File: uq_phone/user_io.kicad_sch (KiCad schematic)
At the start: 27 parts, among them J7 Conn_01x02, J8 KP15B-6S-SF_800_, J9 541324562, M1 VCDM0834B004L, U10 TPD3F303DQDR, U11 TPD8F003DQDR, U12 MCP1664T-E/OT, U8 LSM6DSVTR, U9 DRV2603RUNR

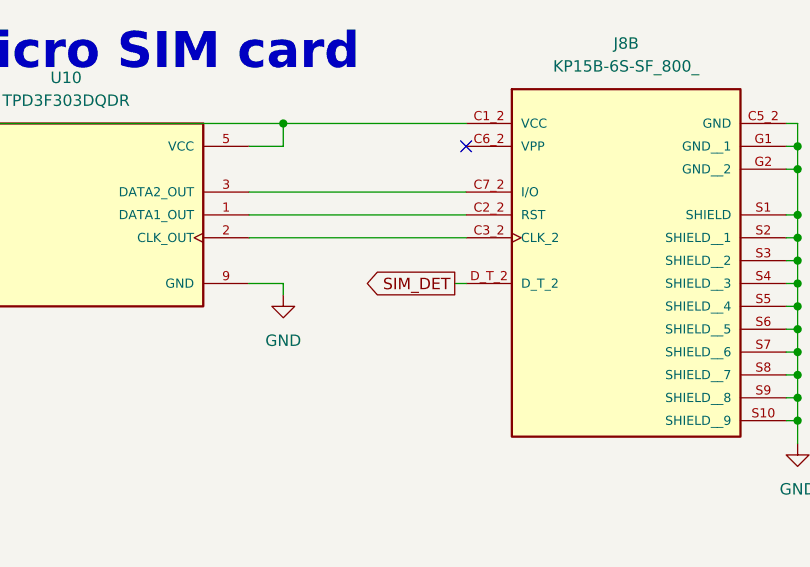
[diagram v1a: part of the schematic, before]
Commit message: Update pcb and remove Stm32 profile
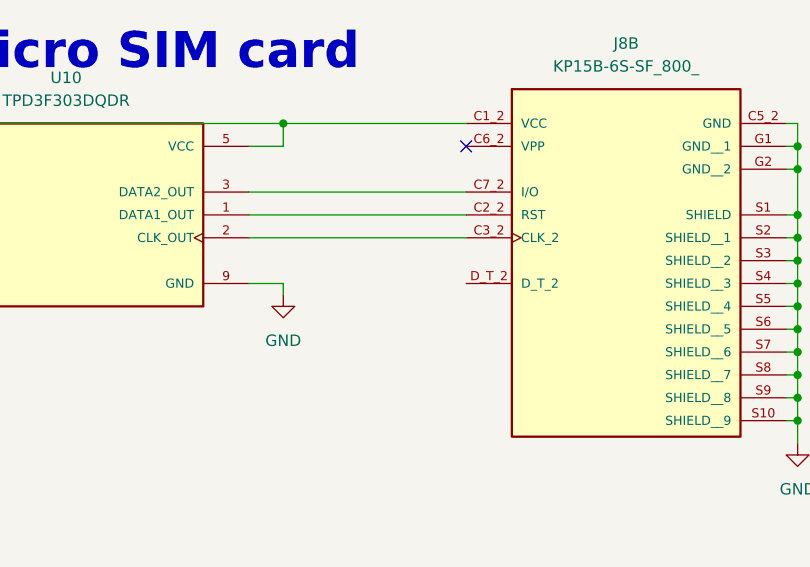
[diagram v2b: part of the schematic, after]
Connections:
- net SIM_DET: no longer names the net of J8.D_T_2
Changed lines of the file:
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@@
-	(wire
-		(pts
-			(xy 175.26 143.51) (xy 176.53 143.51)
-		)
-		(stroke
-			(width 0)
-			(type default)
-		)
-	)
 	(wire
 		(pts
@@
 			(effects
 				(font
-					(size 1.27 1.27)
-				)
-				(justify right)
-				(hide yes)
-			)
-		)
-	)
-	(global_label "SIM_DET"
-		(shape output)
-		(at 175.26 143.51 180)
-		(fields_autoplaced yes)
-		(effects
-			(font
-				(size 1.27 1.27)
-			)
-			(justify right)
-		)
-		(property "Intersheetrefs" "${INTERSHEET_REFS}"
-			(at 164.6549 143.51 0)
-			(effects
-				(font

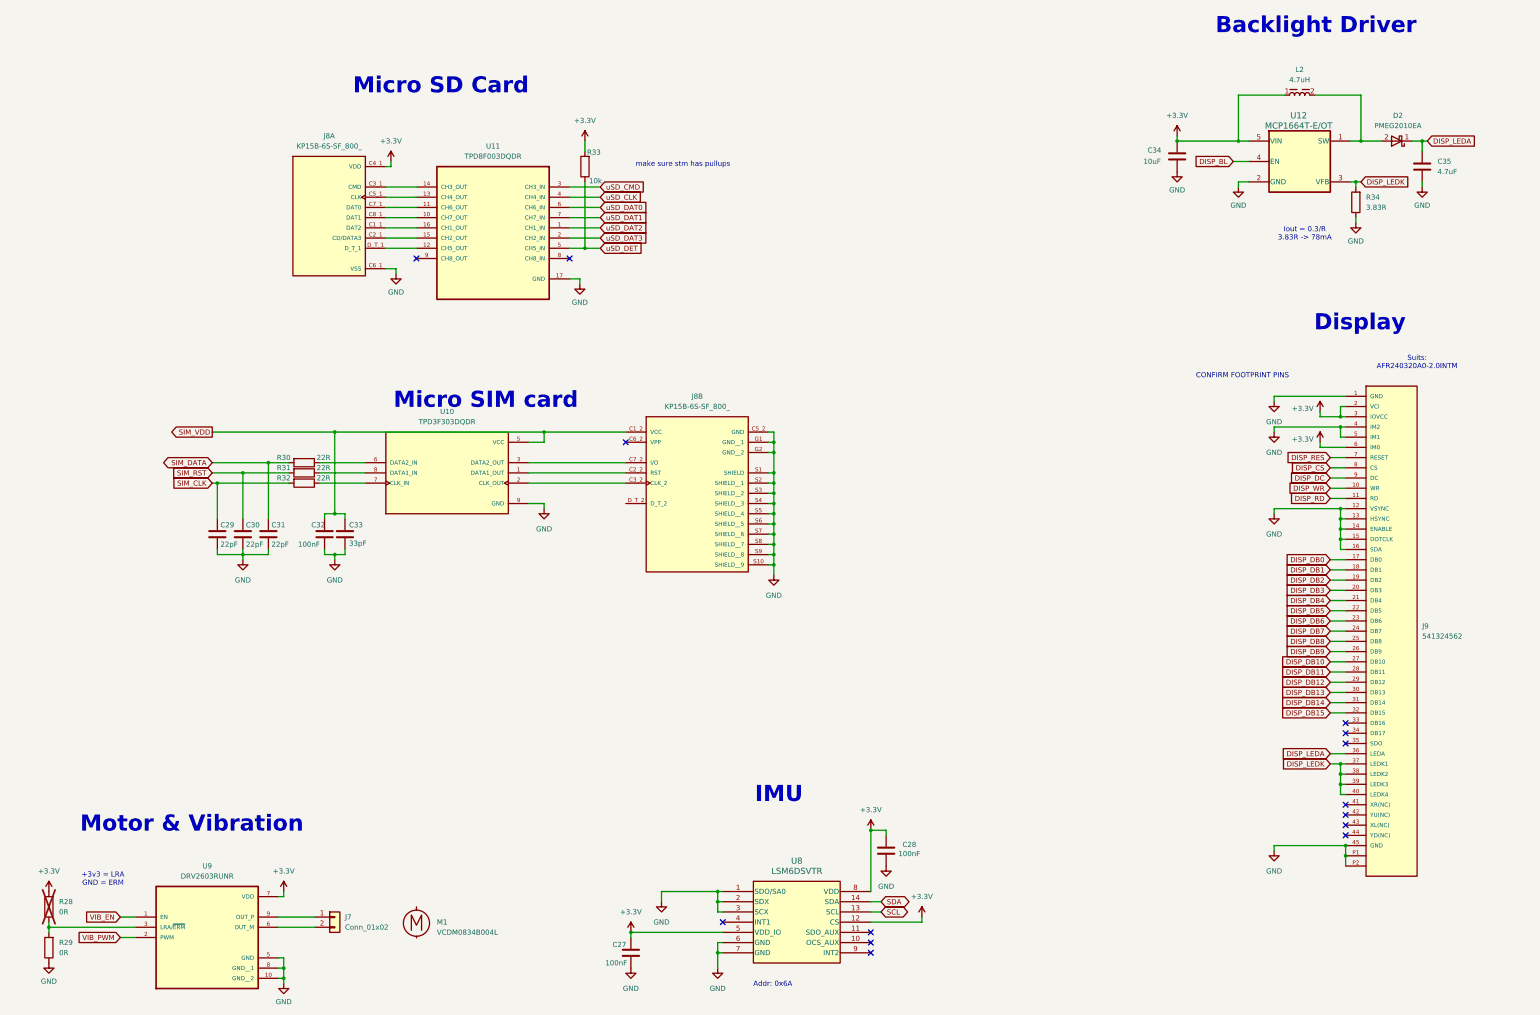
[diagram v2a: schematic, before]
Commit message: Add Front Pannel Suboard and connector
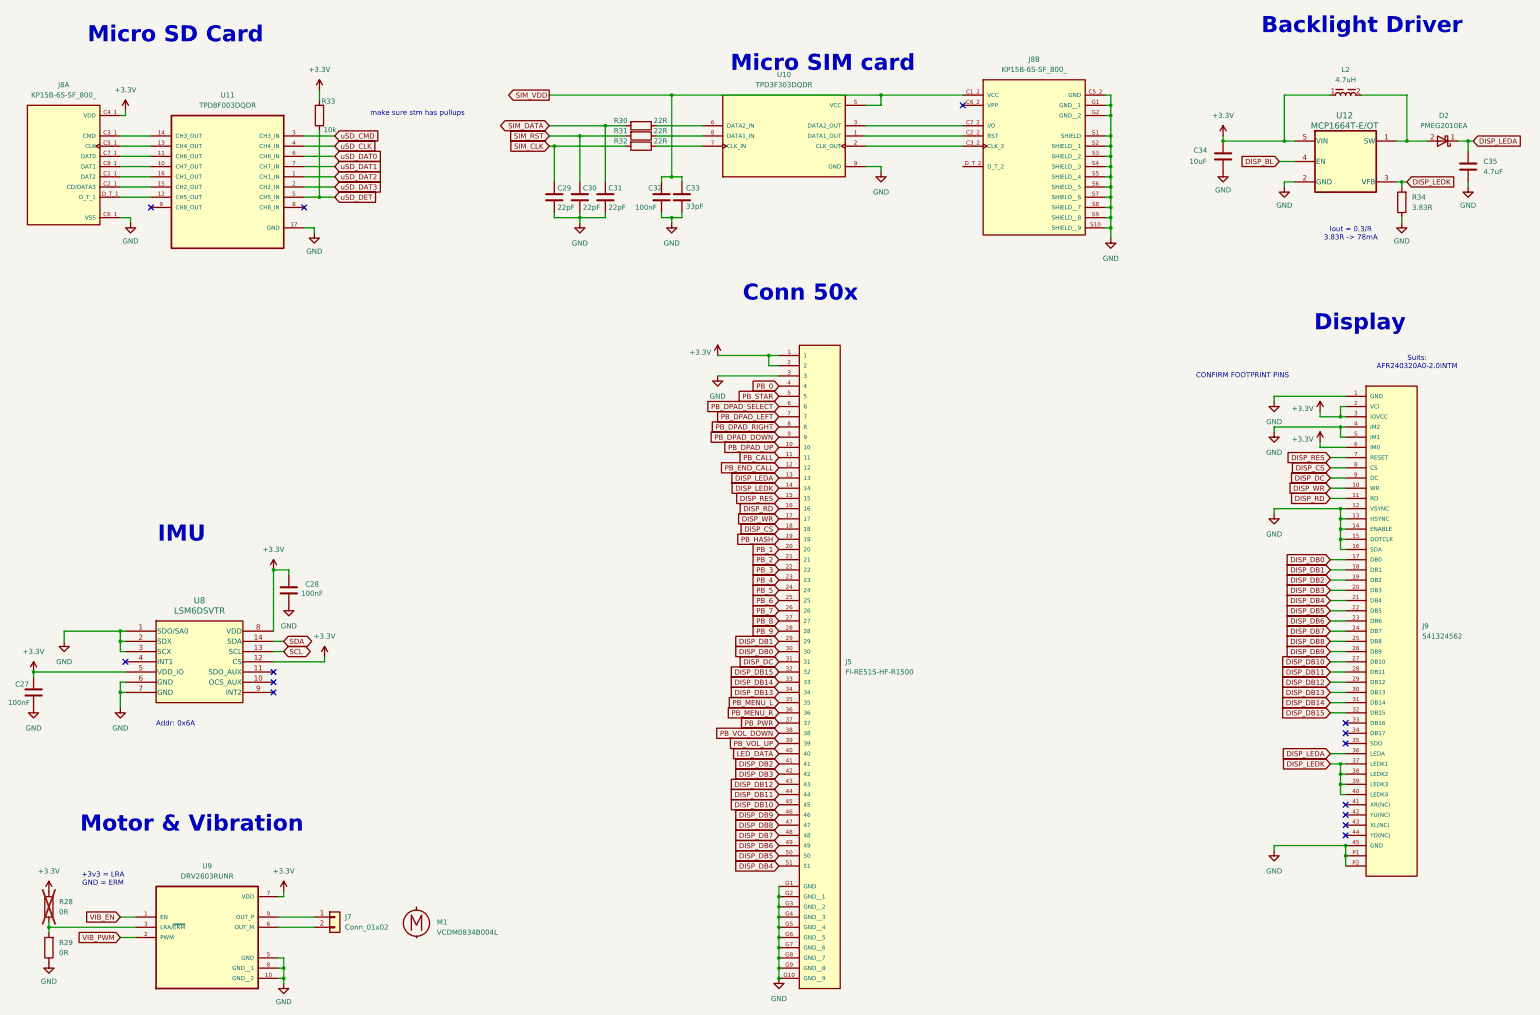
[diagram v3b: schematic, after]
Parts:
- added J5: FI-RE51S-HF-R1500, FI-RE51S-HF-R1500:JAE_FI-RE51S-HF-R1500, symbol FI-RE51S-HF-R1500:FI-RE51S-HF-R1500
- J9: now left out of the parts list
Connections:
- net +3.3V: now also J5.1, J5.2
- net DISP_CS: now also J5.18
- net DISP_DB0: now also J5.30
- net DISP_DB1: now also J5.29
- net DISP_DB10: now also J5.45
- net DISP_DB11: now also J5.44
- net DISP_DB12: now also J5.43
- net DISP_DB13: now also J5.34
- net DISP_DB14: now also J5.33
- net DISP_DB15: now also J5.32
- net DISP_DB2: now also J5.41
- net DISP_DB3: now also J5.42
- net DISP_DB4: now also J5.51
- net DISP_DB5: now also J5.50
- net DISP_DB6: now also J5.49
- net DISP_DB7: now also J5.48
- net DISP_DB8: now also J5.47
- net DISP_DB9: now also J5.46
- net DISP_DC: now also J5.31
- net DISP_LEDA: now also J5.13
- net DISP_LEDK: now also J5.14
- net DISP_RD: now also J5.16
- net DISP_RES: now also J5.15
- net DISP_WR: now also J5.17
- net GND: now also J5.3, J5.G1 (GND), J5.G10 (GND__9), J5.G2 (GND__1), J5.G3 (GND__2), J5.G4 (GND__3), J5.G5 (GND__4), J5.G6 (GND__5), J5.G7 (GND__6), J5.G8 (GND__7), J5.G9 (GND__8)
- new net LED_DATA: J5.40
- new net PB_0: J5.4
- new net PB_1: J5.20
- new net PB_2: J5.21
- new net PB_3: J5.22
- new net PB_4: J5.23
- new net PB_5: J5.24
- new net PB_6: J5.25
- new net PB_7: J5.26
- new net PB_8: J5.27
- new net PB_9: J5.28
- new net PB_CALL: J5.11
- new net PB_DPAD_DOWN: J5.9
- new net PB_DPAD_LEFT: J5.7
- new net PB_DPAD_RIGHT: J5.8
- new net PB_DPAD_SELECT: J5.6
- new net PB_DPAD_UP: J5.10
- new net PB_END_CALL: J5.12
- new net PB_HASH: J5.19
- new net PB_MENU_L: J5.35
- new net PB_MENU_R: J5.36
- new net PB_PWR: J5.37
- new net PB_STAR: J5.5
- new net PB_VOL_DOWN: J5.38
- new net PB_VOL_UP: J5.39
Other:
- note added: "Conn 50x"
- moved on the sheet: C27, C28, C29, C30, C31, C32, C33, C34, C35, D2, J8A, J8B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

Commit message: Clean up and add DNP
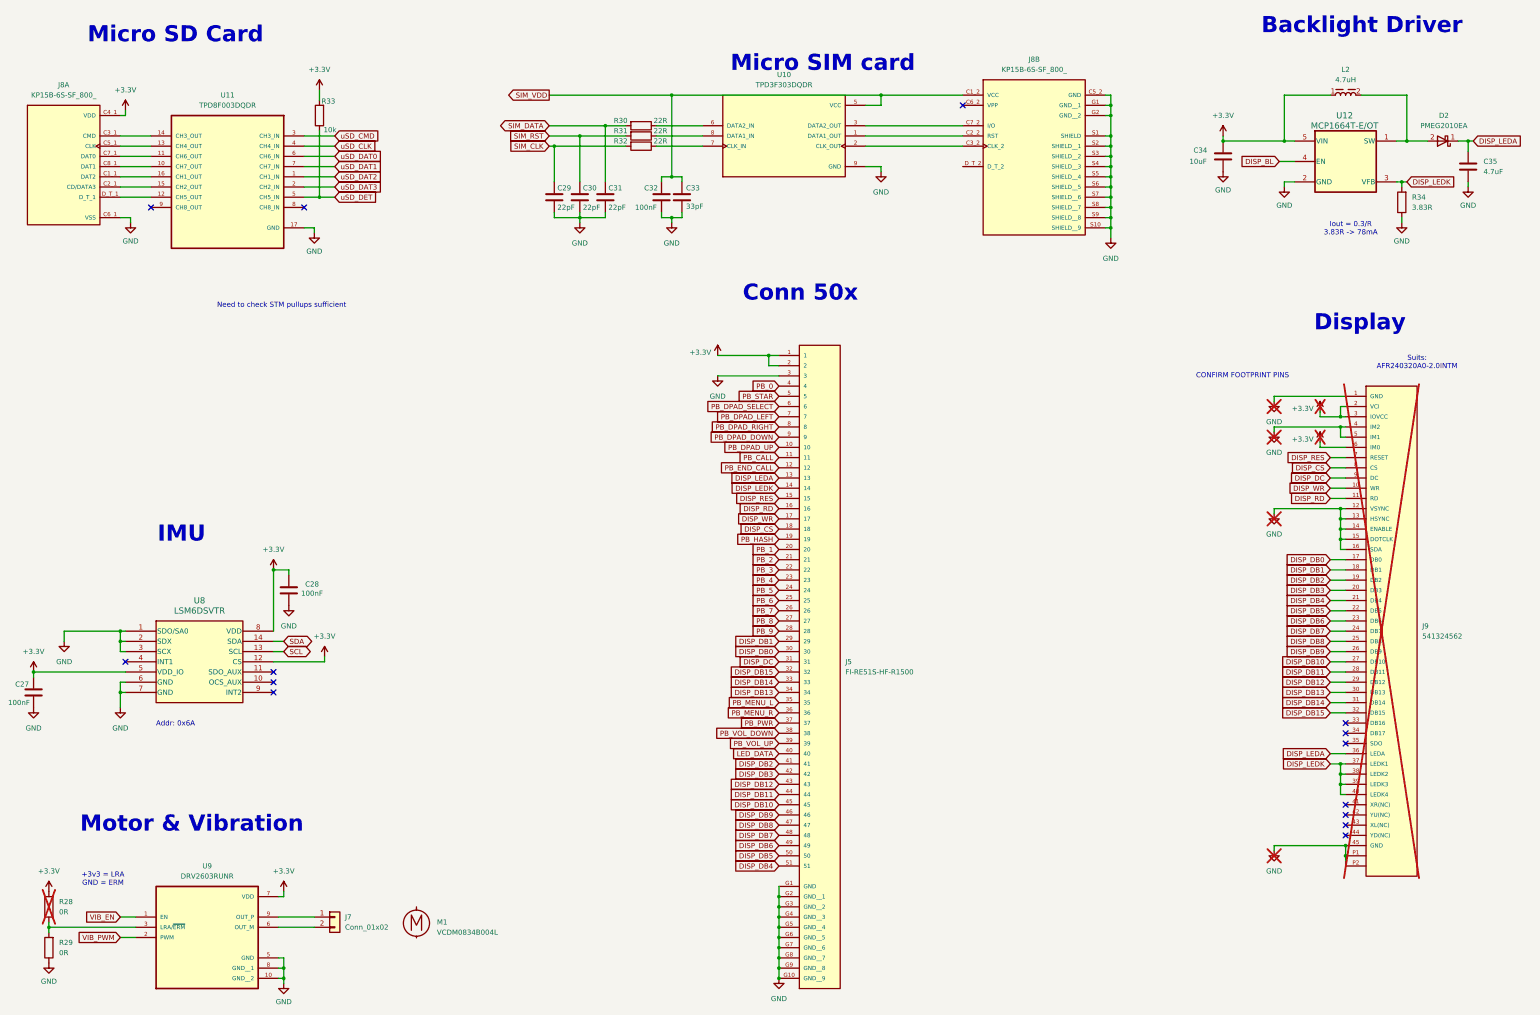
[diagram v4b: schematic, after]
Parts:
- J9: now not fitted
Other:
- note added: "Need to check STM pullups sufficient"
- note removed: "make sure stm has pullups"
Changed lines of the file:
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@@
 		)
 	)
-	(text "make sure stm has pullups\n"
+	(text "Need to check STM pullups sufficient \n"
 		(exclude_from_sim no)
-		(at 124.714 46.482 0)
+		(at 90.932 94.234 0)
 		(effects
 			(font
@@
 	(text "Iout = 0.3/R\n3.83R -> 78mA"
 		(exclude_from_sim no)
-		(at 356.87 76.454 0)
+		(at 356.87 75.184 0)
 		(effects
 			(font
@@
 		(in_bom no)
 		(on_board no)
-		(dnp no)
+		(dnp yes)
 		(fields_autoplaced yes)
 		(property "Reference" "J9"
@@
 		(dnp no)
 		(property "Reference" "C32"
-			(at 182.118 65.024 0)
+			(at 181.102 65.024 0)
 			(effects
 				(font
@@
 		(in_bom no)
 		(on_board no)
-		(dnp no)
+		(dnp yes)
 		(fields_autoplaced yes)
 		(property "Reference" "#PWR094"
@@
 		(in_bom no)
 		(on_board no)
-		(dnp no)
+		(dnp yes)
 		(fields_autoplaced yes)
 		(property "Reference" "#PWR091"
@@
 		(in_bom no)
 		(on_board no)
-		(dnp no)
+		(dnp yes)
 		(property "Reference" "#PWR095"
 			(at 349.25 124.46 0)
@@
 		(in_bom no)
 		(on_board no)
-		(dnp no)
+		(dnp yes)
 		(property "Reference" "#PWR096"
 			(at 349.25 132.08 0)
@@
 		(in_bom no)
 		(on_board no)
-		(dnp no)
+		(dnp yes)
 		(fields_autoplaced yes)
 		(property "Reference" "#PWR092"
@@
 		(in_bom no)
 		(on_board no)
-		(dnp no)
+		(dnp yes)
 		(fields_autoplaced yes)
 		(property "Reference" "#PWR093"

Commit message: Update Various Connectors
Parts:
- removed J5: FI-RE51S-HF-R1500, FI-RE51S-HF-R1500:JAE_FI-RE51S-HF-R1500, symbol FI-RE51S-HF-R1500:FI-RE51S-HF-R1500
- added C50, Cable1: 0151660555, symbol Misc:Cable
- added J5: 6871XX14022_68715014022, 6871XX14022_68715014022:68715014022, symbol 6871XX14022_68715014022:6871XX14022_68715014022
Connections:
- net +3.3V: now also J5.1
- net DISP_CS: now also J5.17
- net DISP_DB0: now also J5.29
- net DISP_DB1: now also J5.28
- net DISP_DB10: now also J5.44
- net DISP_DB11: now also J5.43
- net DISP_DB12: now also J5.42
- net DISP_DB13: now also J5.33
- net DISP_DB14: now also J5.32
- net DISP_DB15: now also J5.31
- net DISP_DB2: now also J5.40
- net DISP_DB3: now also J5.41
- net DISP_DB4: now also J5.50
- net DISP_DB5: now also J5.49
- net DISP_DB6: now also J5.48
- net DISP_DB7: now also J5.47
- net DISP_DB8: now also J5.46
- net DISP_DB9: now also J5.45
- net DISP_DC: now also J5.30
- net DISP_LEDA: now also J5.12
- net DISP_LEDK: now also J5.13
- net DISP_RD: now also J5.15
- net DISP_RES: now also J5.14
- net DISP_WR: now also J5.16
- net GND: now also J5.2, J5.Z1, J5.Z2
- net LED_DATA: now also J5.39
- net PB_0: now also J5.3
- net PB_1: now also J5.19
- net PB_2: now also J5.20
- net PB_3: now also J5.21
- net PB_4: now also J5.22
- net PB_5: now also J5.23
- net PB_6: now also J5.24
- net PB_7: now also J5.25
- net PB_8: now also J5.26
- net PB_9: now also J5.27
- net PB_CALL: now also J5.10
- net PB_DPAD_DOWN: now also J5.8
- net PB_DPAD_LEFT: now also J5.6
- net PB_DPAD_RIGHT: now also J5.7
- net PB_DPAD_SELECT: now also J5.5
- net PB_DPAD_UP: now also J5.9
- net PB_END_CALL: now also J5.11
- net PB_HASH: now also J5.18
- net PB_MENU_L: now also J5.34
- net PB_MENU_R: now also J5.35
- net PB_PWR: now also J5.36
- net PB_STAR: now also J5.4
- net PB_VOL_DOWN: now also J5.37
- net PB_VOL_UP: now also J5.38

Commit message: Generate Early production outputs
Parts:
- removed C50: 0151660555, symbol Misc:Cable
- C27, C28, C32: LCSC PN (none) -> C307331
- C29, C30, C31: LCSC PN (none) -> C2168187
- C33: LCSC PN (none) -> C70465
- C34: LCSC PN (none) -> C2168196
- C35: LCSC PN (none) -> C191541
- D2: LCSC PN (none) -> C193668
- L2: LCSC PN (none) -> C2761891
- M1: now not fitted
- R28, R29: LCSC PN (none) -> C95177
- R30, R31, R32: LCSC PN (none) -> C6117700
- R33: LCSC PN (none) -> C851848
- R34: LCSC PN (none) -> C3037044
- U10: LCSC PN (none) -> C2869050
- U11: LCSC PN (none) -> C473368
- U12: LCSC PN (none) -> C625339
- U9: Description_1 Haptic driver for ERM/LRA with auto-resonance tracking in QFN package -> Haptic driver for ERM/LRA with auto-resonance tracking in QFN package; LCSC PN (none) -> C75424
